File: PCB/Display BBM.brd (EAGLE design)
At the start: 100 x 80 mm, 9 parts, among them IC1 MEGA8-AI, IC2 7805DT

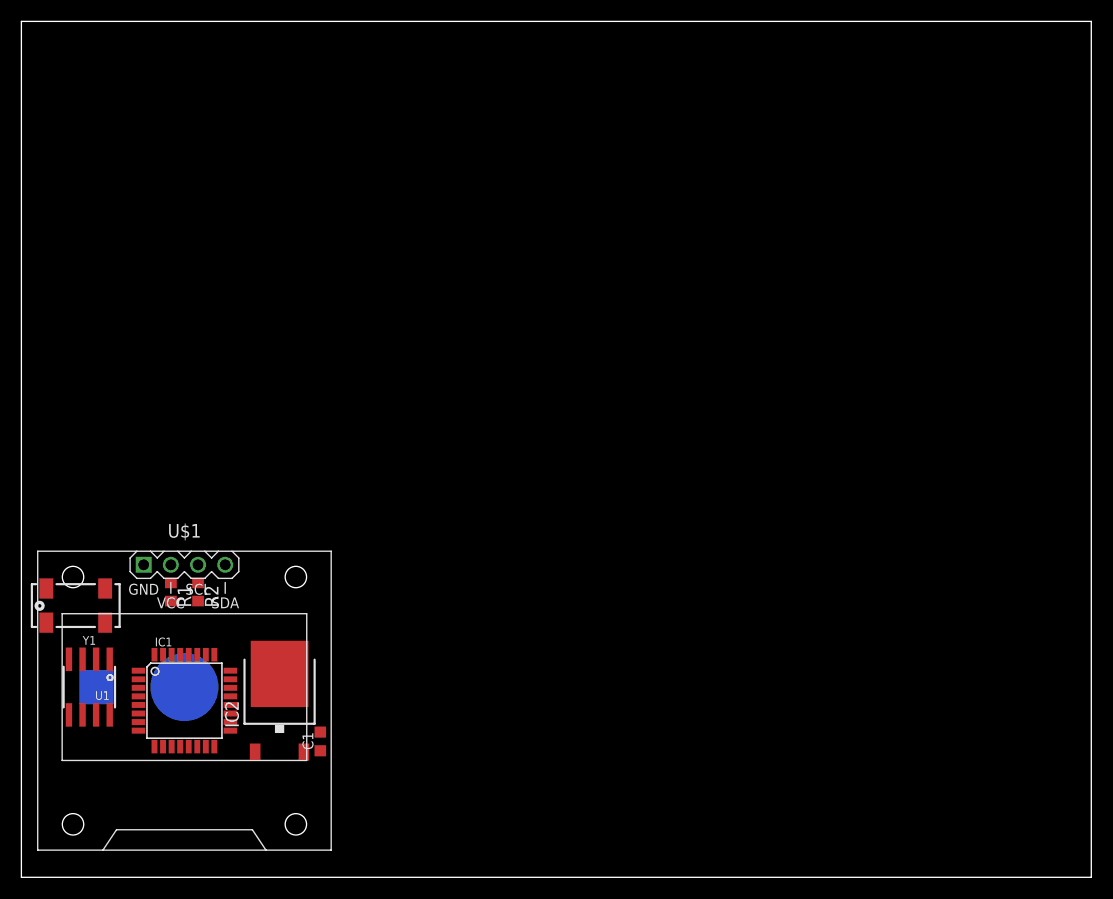
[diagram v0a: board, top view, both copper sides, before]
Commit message: Schematic and Layout V 1.0
Needs to tidy up the layout
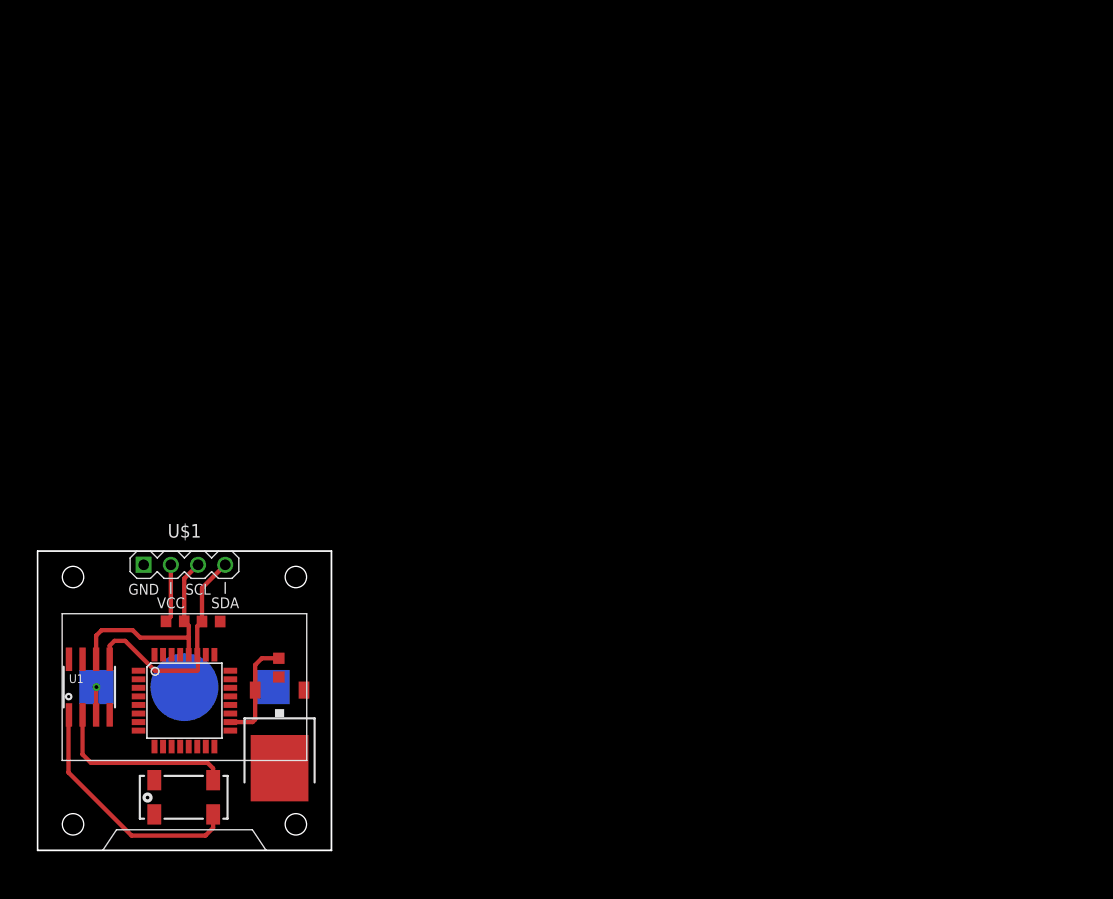
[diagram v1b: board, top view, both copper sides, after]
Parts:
- moved Y1 20.6 mm to (15.2, 7.48)
- moved C1 7.92 mm to (24.1, 19.6), turned to 270 degrees
- moved IC2 3.81 mm to (24.1, 12.7), turned to 180 degrees
- moved R2 3.02 mm to (17.7, 23.9), turned to 0 degrees
- moved R1 2.77 mm to (14.4, 23.9), turned to 180 degrees
- turned U1 to 0 degrees
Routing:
- net X1: track 0.00 -> 22.9 mm
- net SDA: track 0.00 -> 21.8 mm
- net SCL: track 0.00 -> 20.5 mm
- net X2: track 0.00 -> 17.5 mm
- net VCC: track 0.00 -> 15.5 mm
- net VBATT: track 0.00 -> 2.61 mm, vias 0 -> 1
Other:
- board size 100 x 80 mm -> 27.5 x 28 mm

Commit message: Add Scheme and Layout V 2.0
Haven't place a voltage divider
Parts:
- added X1: (no value), atmel:IDC-06V
- moved C1 13.2 mm to (18.5, 7.70)
- moved IC2 11.7 mm to (13.6, 7.67), turned to 90 degrees
- moved Y1 10.3 mm to (5.12, 9.87), turned to 270 degrees
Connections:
- removed net X1: U1.1, Y1.P$4
- removed net X2: U1.2, Y1.P$1
- new net N$2: U1.1, Y1.P$1
- new net N$3: U1.2, Y1.P$4
- net GND: now also X1.6
- net MISO: now also X1.1
- net MOSI: now also X1.4
- net RST: now also X1.5
- net SCK: now also X1.3
- net VCC: now also X1.2
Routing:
- net RST: track 0.00 -> 63.6 mm, vias 0 -> 2
- net VCC: track 15.5 -> 77.8 mm
- net X1: track 22.9 -> 0.00 mm
- net GND: track 0.00 -> 21.6 mm, vias 0 -> 2
- net X2: track 17.5 -> 0.00 mm
- net SCK: track 0.00 -> 10.7 mm
- net MOSI: track 0.00 -> 9.93 mm
- net SDA: track 21.8 -> 31.1 mm, vias 0 -> 2
- net MISO: track 0.00 -> 5.77 mm
- net N$3: track 0.00 -> 2.98 mm
- net N$2: track 0.00 -> 2.94 mm
- net SCL: track 20.5 -> 19.6 mm
- added copper zone on layer 1, net GND
- added copper zone on layer 16, net GND
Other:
- board size 27.5 x 28 mm -> 28.1 x 28.7 mm
